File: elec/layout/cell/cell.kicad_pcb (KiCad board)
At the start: 2 copper layers, 5 parts

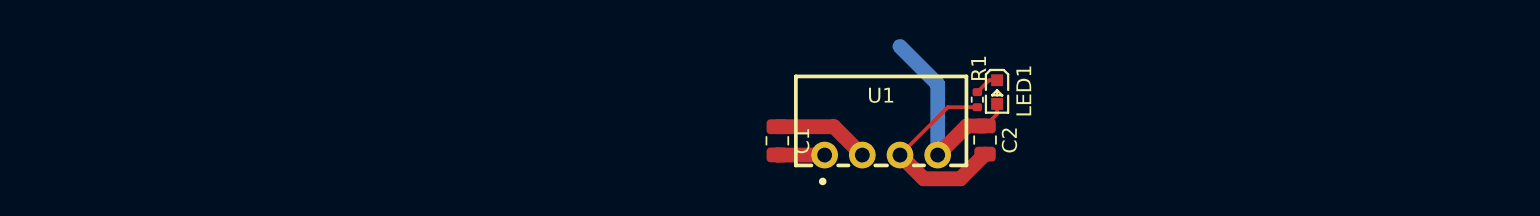
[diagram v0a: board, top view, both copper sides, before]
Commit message: single cell design + layout complete
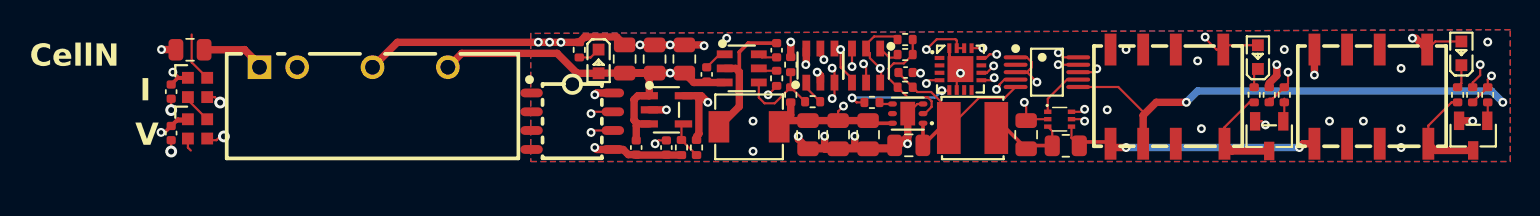
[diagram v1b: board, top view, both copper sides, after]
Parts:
- added C10: 25V 1uF X5R ±10% 0402 Multilayer Ceramic Capacitors MLCC - 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, lib:C0402, F.Cu at (151.8, 98.1)
- added C11: 25V 10uF X5R ±10% 0805 Multilayer Ceramic Capacitors MLCC -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, lib:C0805, F.Cu at (152.0, 103.0)
- added C12: 25V 10uF X5R ±10% 0805 Multilayer Ceramic Capacitors MLCC -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, lib:C0805, F.Cu at (159.9, 102.3)
- added C13: 16V 100nF X7R ±10% 0402 Multilayer Ceramic Capacitors MLCC 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, lib:C0402, F.Cu at (102.2, 102.2)
- added C14: 16V 100nF X7R ±10% 0402 Multilayer Ceramic Capacitors MLCC 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, lib:C0402, F.Cu at (102.2, 99.4)
- added C15: 25V 1uF X5R ±10% 0402 Multilayer Ceramic Capacitors MLCC - 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, lib:C0402, F.Cu at (133.6, 103.1)
- added C16: 25V 1uF X5R ±10% 0402 Multilayer Ceramic Capacitors MLCC - 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, lib:C0402, F.Cu at (135.6, 103.1)
- added C3: 25V 10uF X5R ±10% 0805 Multilayer Ceramic Capacitors MLCC -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, lib:C0805, F.Cu at (136.8, 97.2)
- added C4: 25V 10uF X5R ±10% 0805 Multilayer Ceramic Capacitors MLCC -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, lib:C0805, F.Cu at (134.8, 97.2)
- added C5: 16V 100nF X7R ±10% 0402 Multilayer Ceramic Capacitors MLCC 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, lib:C0402, F.Cu at (138.4, 98.2)
- added C6: 25V 10uF X5R ±10% 0805 Multilayer Ceramic Capacitors MLCC -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, lib:C0805, F.Cu at (147.2, 102.3)
- added C7: 25V 10uF X5R ±10% 0805 Multilayer Ceramic Capacitors MLCC -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, lib:C0805, F.Cu at (149.2, 102.3)
- added C8: 25V 10uF X5R ±10% 0805 Multilayer Ceramic Capacitors MLCC -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, lib:C0805, F.Cu at (145.2, 102.3)
- added C9: 16V 100nF X7R ±10% 0402 Multilayer Ceramic Capacitors MLCC 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, lib:C0402, F.Cu at (143.1, 96.6)
- added L1: , lib:IND-SMD_L4.4-W4.2, F.Cu at (141.2, 101.7)
- added L2: 100uH, lib:IND-SMD_L4.0-W4.0, F.Cu at (156.3, 101.8)
- added LED2: , lib:LED0603-RD, F.Cu at (175.5, 97.0)
- added LED3: , lib:LED0603-RD, F.Cu at (189.2, 96.8)
- added Q1: , lib:SOT-23-3_L2.9-W1.3-P1.90-LS2.4-BR, F.Cu at (176.3, 102.4)
- added Q2: , lib:SOT-23-3_L2.9-W1.3-P1.90-LS2.4-BR, F.Cu at (190.0, 102.3)
- added R10: 125mW Thick Film Resistors 150V ±1% 100mΩ 0805 Chip Resisto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, lib:R0805, F.Cu at (162.6, 103.0)
- added R11: 62.5mW Thick Film Resistors 50V ±100ppm/℃ ±1% 21kΩ 0402 Chi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, lib:R0402, F.Cu at (175.3, 99.6)
- added R12: 62.5mW Thick Film Resistors 50V ±100ppm/℃ ±1% 10kΩ 0402 Chi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, lib:R0402, F.Cu at (177.3, 99.6)
- added R13: 62.5mW Thick Film Resistors 50V ±100ppm/℃ ±1% 1kΩ 0402 Chip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, lib:R0402, F.Cu at (176.3, 99.6)
- added R14: 62.5mW Thick Film Resistors 50V ±100ppm/℃ ±1% 21kΩ 0402 Chi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, lib:R0402, F.Cu at (189.0, 99.6)
- added R15: 62.5mW Thick Film Resistors 50V ±100ppm/℃ ±1% 10kΩ 0402 Chi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, lib:R0402, F.Cu at (191.0, 99.6)
- added R16: 62.5mW Thick Film Resistors 50V ±100ppm/℃ ±1% 1kΩ 0402 Chip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, lib:R0402, F.Cu at (190.0, 99.6)
- added R17: 62.5mW Thin Film Resistor 50V ±25ppm/℃ ±1% 11.5kΩ 0402 Chip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, lib:R0402, F.Cu at (137.7, 103.1)
- added R18: 62.5mW Thick Film Resistors 50V ±100ppm/℃ ±1% 6.2kΩ 0402 Ch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, lib:R0402, F.Cu at (136.7, 103.1)
- added R2: 62.5mW Thick Film Resistors 50V ±100ppm/℃ ±1% 24kΩ 0402 Chi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, lib:R0402, F.Cu at (145.5, 100.0)
- added R3: 62.5mW Thick Film Resistors 50V ±100ppm/℃ ±1% 37.4kΩ 0402 C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, lib:R0402, F.Cu at (144.0, 99.6)
- added R4: 62.5mW Thick Film Resistors 50V ±100ppm/℃ ±1% 10kΩ 0402 Chi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, lib:R0402, F.Cu at (144.0, 97.5)
- added R5: 62.5mW Thick Film Resistors 50V ±100ppm/℃ ±1% 10kΩ 0402 Chi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, lib:R0402, F.Cu at (143.1, 98.5)
- added R6: 62.5mW Thick Film Resistors 50V ±100ppm/℃ ±1% 43kΩ 0402 Chi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, lib:R0402, F.Cu at (151.7, 96.9)
- added R7: 62.5mW Thick Film Resistors 50V ±100ppm/℃ ±1% 60.4kΩ 0402 C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, lib:R0402, F.Cu at (151.7, 99.1)
- added R8: 62.5mW Thick Film Resistors 50V ±100ppm/℃ ±1% 10kΩ 0402 Chi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, lib:R0402, F.Cu at (151.7, 95.8)
- added R9: 62.5mW Thick Film Resistors 50V ±100ppm/℃ ±1% 10kΩ 0402 Chi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, lib:R0402, F.Cu at (149.5, 100.1)
- added U10: , lib:QFN-16_L3.0-W3.0-P0.50-BL-EP1.7, F.Cu at (155.5, 97.8)
- added U11: , lib:SOIC-8_L4.9-W3.9-P1.27-LS6.0-TL, F.Cu at (129.3, 101.3)
- added U12: , lib:LED-SMD_4P-L2.0-W2.0-BR, F.Cu at (104.0, 101.9)
- added U13: , lib:LED-SMD_4P-L2.0-W2.0-BR, F.Cu at (104.0, 99.1)
- added U14: , lib:SOT-23-5_L3.0-W1.7-P0.95-LS2.8-BL, F.Cu at (135.6, 100.6)
- added U2: , lib:MSOP-10_L3.0-W3.0-P0.50-LS5.0-BL, F.Cu at (161.3, 98.0)
- added U3: , lib:SOT-23-6_L2.9-W1.6-P0.95-LS2.8-BL, F.Cu at (146.0, 97.6)
- added U4: , lib:SOT-23-6_L2.9-W1.6-P0.95-LS2.8-BL, F.Cu at (140.7, 97.8)
- added U5: , lib:SOT-23-6_L2.9-W1.6-P0.95-LS2.8-BL, F.Cu at (149.1, 97.6)
- added U6: , lib:WSON-6_L2.0-W2.0-P0.65-TL-EP, F.Cu at (151.9, 100.8)
- added U7: , lib:SOT-563_L1.6-W1.2-P0.50-LS1.6-TL, F.Cu at (162.1, 101.2)
- added U8: , lib:RELAY-SMD_HFD4-5-SR, F.Cu at (169.4, 99.7)
- added U9: , lib:RELAY-SMD_HFD4-5-SR, F.Cu at (183.2, 99.7)
- R1: value 62.5mW Thick Film Resistors 50V ±100ppm/℃ ±1% 3.48kΩ 0402 Chip Resistor - Surface Mount ROHS -> 62.5mW Thick Film Resistors 50V ±100ppm/℃ ±1% 21kΩ 0402 Chip Resistor - Surface Mount ROHS
- U1: footprint lib:PWRM-TH_YLPTEC_BXXXXS-1WR3 -> lib:PWRM-TH_BXXXXS-2WR2
- moved C1 40.1 mm to (103.5, 96.5), turned to 180 degrees
- moved U1 36.1 mm to (114.6, 97.7)
- moved R1 27.0 mm to (129.8, 96.5), turned to 90 degrees
- moved LED1 26.9 mm to (131.1, 97.3)
- moved C2 24.9 mm to (132.8, 97.2), turned to 90 degrees
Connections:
- net cathode renamed isolated_converter.led.resistor-cathode
- C2 pad 1: vcc-1 -> vcc-6
- C2 pad 2: gnd-1 -> gnd-6
- LED1 pad 2: vcc-1 -> vcc-6
- R1 pad 2: gnd-1 -> gnd-6
- U1 pad 1: gnd -> vcc
- U1 pad 2: vcc -> gnd
- U1 pad 4: vcc-1 -> gnd-6
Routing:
- net vcc-6: track 0.00 -> 87.6 mm, vias 0 -> 3
- net gnd-6: track 0.00 -> 84.9 mm, vias 0 -> 40
- net scl-1: track 0.00 -> 43.3 mm, vias 0 -> 5
- net sda-1: track 0.00 -> 40.6 mm, vias 0 -> 4
- net dmm_relay-input: track 0.00 -> 38.0 mm, vias 0 -> 2
- net output_relay-input: track 0.00 -> 24.4 mm, vias 0 -> 2
- net adc-vcc: track 0.00 -> 24.4 mm, vias 0 -> 2
- net vcc-1: track 14.2 -> 34.4 mm, vias 0 -> 2
- net current_sense.sensor-vcc: track 0.00 -> 17.7 mm, vias 0 -> 2
- net adc-vcc-1: track 0.00 -> 16.6 mm
- net vcc-7: track 0.00 -> 15.9 mm, vias 0 -> 9
- net gnd-1: track 13.6 -> 0.00 mm
- net buck-enable: track 0.00 -> 12.8 mm, vias 0 -> 2
- net sw: track 0.00 -> 9.46 mm
- net fb: track 0.00 -> 8.56 mm
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- added copper zone on B.Cu, net gnd-6
- added copper zone on F.Cu, net gnd-6
- added copper zone on In2.Cu, net vcc-7
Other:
- copper layers 2 -> 4
- board text added: "CellN"
- board text added: "I"
- board text added: "V"

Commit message: layout progress
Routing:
- net gnd-6: track 84.9 -> 91.9 mm
- removed copper zone on B.Cu, net gnd-6
- removed copper zone on F.Cu, net gnd-6
- removed copper zone on In2.Cu, net vcc-7

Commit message: layout complete
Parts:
- R10: value 125mW Thick Film Resistors 150V ±1% 100mΩ 0805 Chip Resistor - Surface Mount ROHS -> 125mW Thick Film Resistors ±600ppm/℃ ±1% 110mΩ 0805 Chip Resistor - Surface Mount ROHS
- R17: value 62.5mW Thin Film Resistor 50V ±25ppm/℃ ±1% 11.5kΩ 0402 Chip Resistor - Surface Mount ROHS -> 62.5mW Thick Film Resistors 50V ±100ppm/℃ ±1% 11.5kΩ 0402 Chip Resistor - Surface Mount ROHS
- R7: value 62.5mW Thick Film Resistors 50V ±100ppm/℃ ±1% 60.4kΩ 0402 Chip Resistor - Surface Mount ROHS -> 62.5mW Thick Film Resistors 50V ±100ppm/℃ ±1% 59kΩ 0402 Chip Resistor - Surface Mount ROHS
- moved U13 52.1 mm to (57.7, 122.8), turned to 0 degrees
- moved C12 50.2 mm to (114.2, 123.0)
- moved C15 50.2 mm to (87.9, 123.9)
- moved C2 50.2 mm to (87.1, 117.9)
- moved C7 50.2 mm to (103.5, 123.0)
- moved C9 50.2 mm to (97.4, 117.4)
- moved R1 50.2 mm to (84.1, 117.3)
- moved R8 50.2 mm to (106.0, 116.6)
- moved U10 50.2 mm to (109.8, 118.6)
- moved U4 50.2 mm to (95.0, 118.6)
- moved C1 50.2 mm to (57.8, 117.3)
- moved C10 50.2 mm to (106.1, 118.9)
- moved C11 50.2 mm to (106.3, 123.8)
- moved C16 50.2 mm to (89.9, 123.9)
- moved C3 50.2 mm to (91.2, 117.9)
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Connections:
- U10 pad 2: buck-enable -> p0
- U10 pad 3: ldo-enable -> p1
- U10 pad 4: p2 -> buck-enable
- U10 pad 5: p3 -> ldo-enable
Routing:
- net gnd-6: track 91.9 -> 106.6 mm, vias 40 -> 31
- net vcc-2: track 6.16 -> 2.63 mm, vias 2 -> 0
- net led_data: track 0.89 -> 2.99 mm
- net led_data-1: track 3.35 -> 1.40 mm
- added copper zone on B.Cu, net gnd-6
- added copper zone on In1.Cu, net vcc-7
